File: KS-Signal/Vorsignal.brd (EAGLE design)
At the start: 24.6 x 42.3 mm, 10 parts

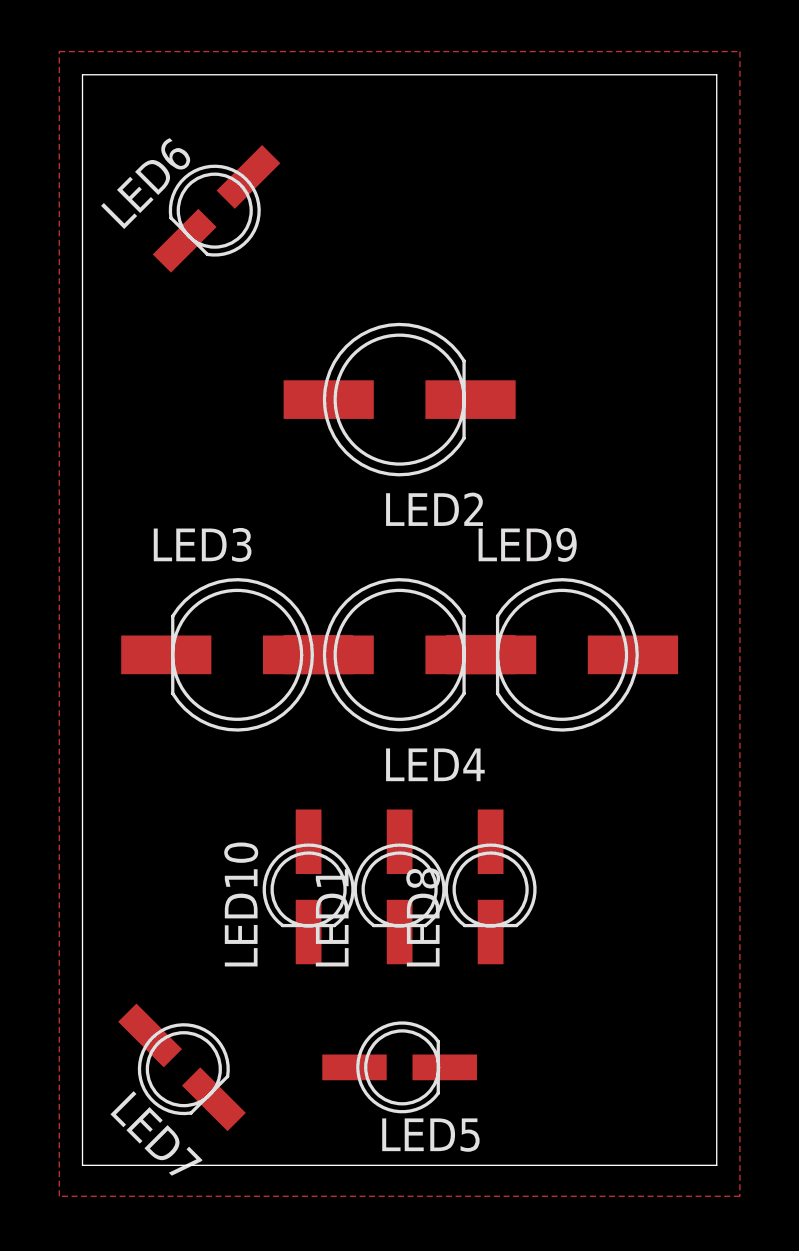
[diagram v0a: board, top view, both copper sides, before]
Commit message: Vorsignale fertiggestellt
- Vorsignalschirme fertiggestellt
- Platinengrößen angepasst
-> Achtung: Stecker und Pinbelegung unterschiedlich zwischen den beiden Vorsignaltypen
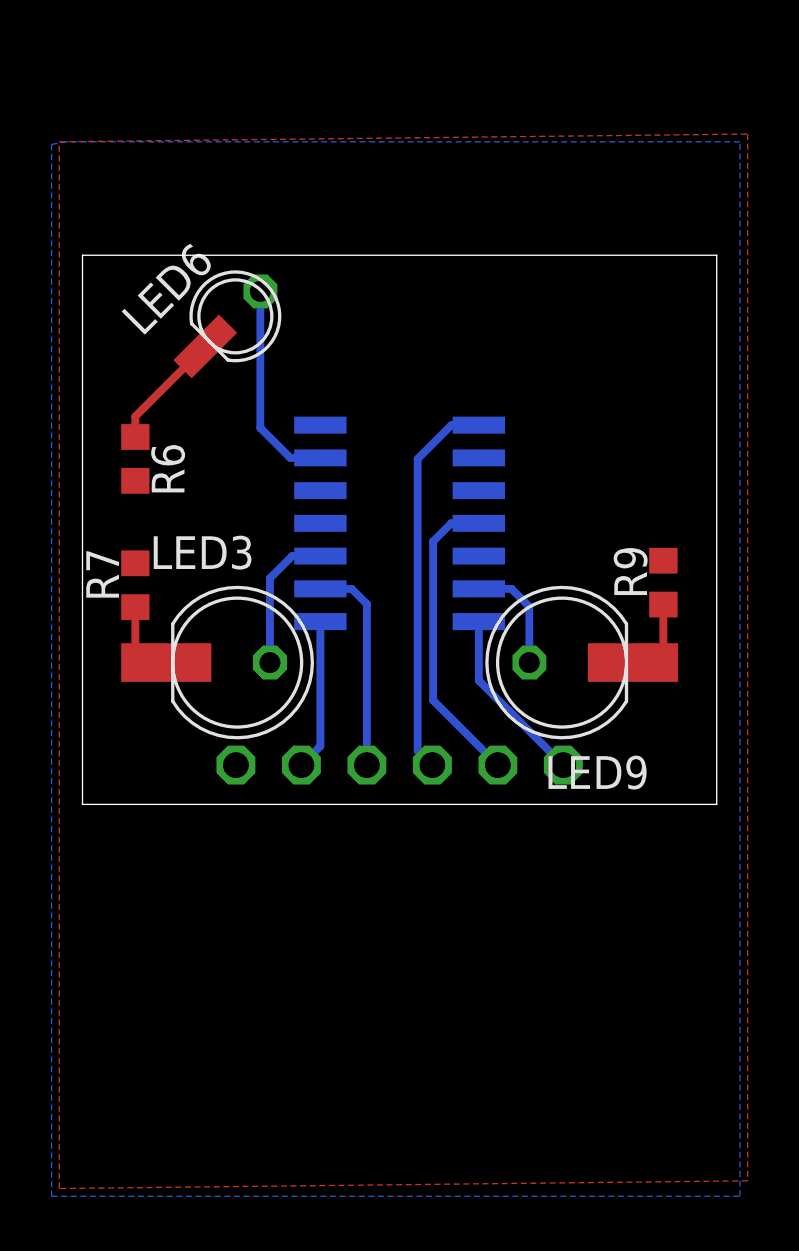
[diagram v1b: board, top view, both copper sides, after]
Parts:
- removed LED1, LED10, LED5, LED7, LED8: LED_SMD3MM, LEDFLATTOP:3MM_FLAT_SMDLED
- removed LED2, LED4: LED_SMD5MM, LEDFLATTOP:5MM_FLAT_SMDLED
- added IC1: ATTINY44SSU, Attiny:SO14
- added R6, R7, R9: (no value), rcl:R0603
- added X2: TSW-106-02-S-S-RA, con-samtec:TSW-106-02-S-S-RA
- LED3, LED9: value LED_SMD5MM -> LED_SMD5MM_SMD/DIP; device LEDFLATTOP:5MM_FLAT_SMDLED -> LEDFLATTOP:5MM_FLAT/DIP_SMDLED
- LED6: value LED_SMD3MM -> LED_SMD3MM_SMD/DIP; device LEDFLATTOP:3MM_FLAT_SMDLED -> LEDFLATTOP:3MM_FLAT/DIP_SMDLED
- moved LED6 4.18 mm to (6.00, 33.0)
- moved LED3 0.30 mm to (6.00, 19.5)
- moved LED9 0.30 mm to (18.6, 19.5), turned to 180 degrees
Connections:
- new net GE: IC1.6, LED9.+
- new net GN: IC1.10, LED3.+
- new net MISO: IC1.8, X2.2
- new net N$2: LED6.-, R6.1
- new net N$8: LED3.-, R7.1
- new net RESET: IC1.4, X2.5
- new net SCL/SCK: IC1.9, X2.3
- new net SDA/MOSI: IC1.7, X2.6
- new net VCC: IC1.1, X2.4
- new net ZL: IC1.13, LED6.+
- net GND: now also IC1.14, R6.2, R7.2, R9.2, X2.1; no longer LED1.-, LED10.-, LED2.-, LED3.-, LED4.-, LED5.-, LED6.-, LED7.-, LED8.-, LED9.-
- net N$1: now also LED9.-, R9.1; no longer LED3.+, LED4.+
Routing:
- net VCC: track 0.00 -> 15.0 mm
- net RESET: track 0.00 -> 11.8 mm
- net SCL/SCK: track 0.00 -> 8.29 mm
- net ZL: track 0.00 -> 8.11 mm
- net SDA/MOSI: track 0.00 -> 6.92 mm
- net MISO: track 0.00 -> 5.87 mm
- net GN: track 0.00 -> 5.58 mm
- net N$2: track 0.00 -> 4.64 mm
- net GE: track 0.00 -> 4.41 mm
- net N$8: track 0.00 -> 3.35 mm
- net N$1: track 0.80 -> 3.43 mm
- added copper zone on layer 16, net GND
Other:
- board size 24.6 x 42.3 mm -> 24.6 x 21.3 mm
